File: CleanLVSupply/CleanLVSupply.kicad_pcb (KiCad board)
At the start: 4 copper layers, 40 x 40 mm, 77 parts, among them J1 12VIN, J2 5V, J3 5V, J4 5V, J5 +-15V, J6 +-15V, U1 LM25576, U2 TPS7A30, U3 LMR64010XMF, U4 TPS7A47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

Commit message: CleanLVSupply fixes, HiFiDAC skeleton
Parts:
- J5, J6: footprint BW_Connectors:Amphenol_MINITEK_0.8_3P_V -> BW_Connectors:Amphenol_MINITEK_0.8_4P_V
- R6: value 10kΩ -> 10kΩLN
- R8: value 118kΩ -> 118kΩLN
- moved C40 0.30 mm to (164.4, 116.2)
- moved C28 0.30 mm to (166.8, 105.8)
- moved C18 0.15 mm to (163.0, 91.1)
- moved C14 0.12 mm to (164.7, 83.5)
- moved J5 0.10 mm to (167.9, 98.4)
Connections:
- J5 pad 3: -15V -> GND
- J6 pad 3: -15V -> GND
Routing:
- net GND: track 138.4 -> 143.9 mm
- net +15V: track 31.2 -> 31.8 mm

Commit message: HiFiDAC schematic initially done, CleanLVSupply added shield pads
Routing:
- net GND: vias 88 -> 87

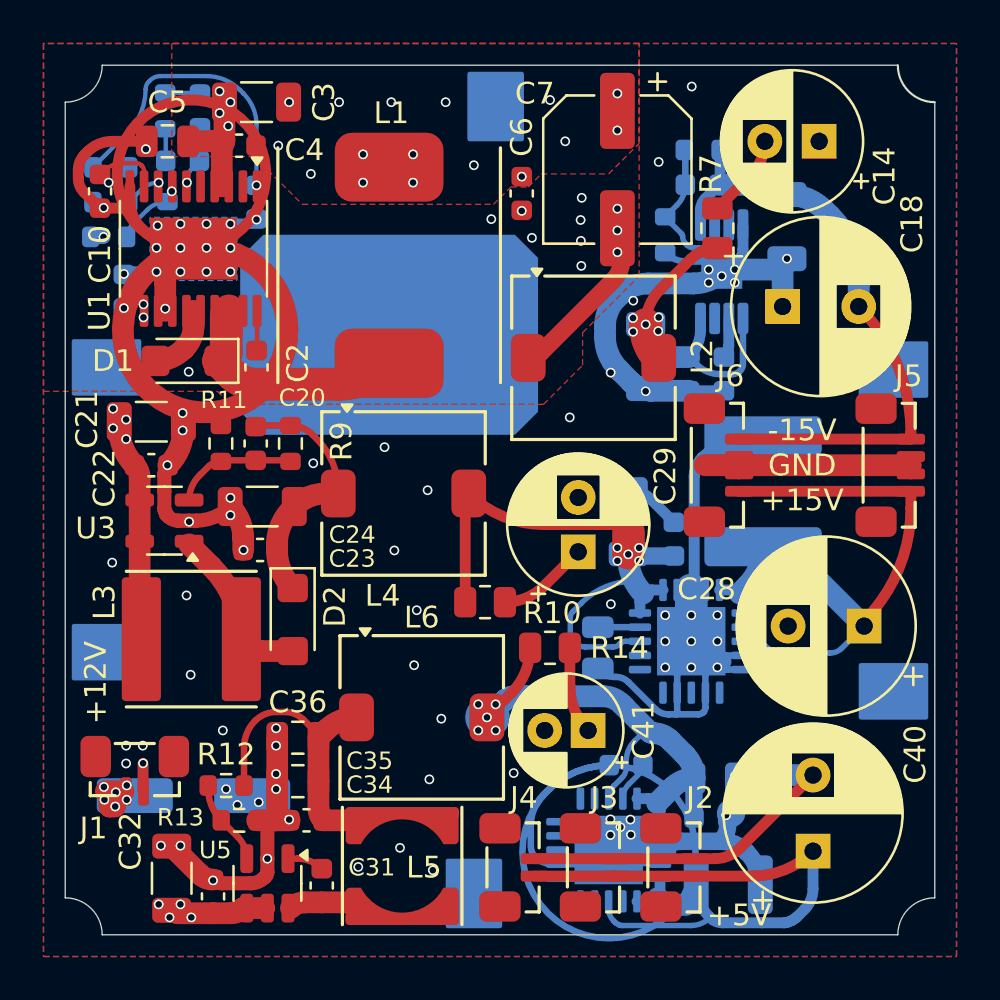
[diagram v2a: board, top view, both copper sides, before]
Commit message: HiFiDAC PCB progress, slight shape changes
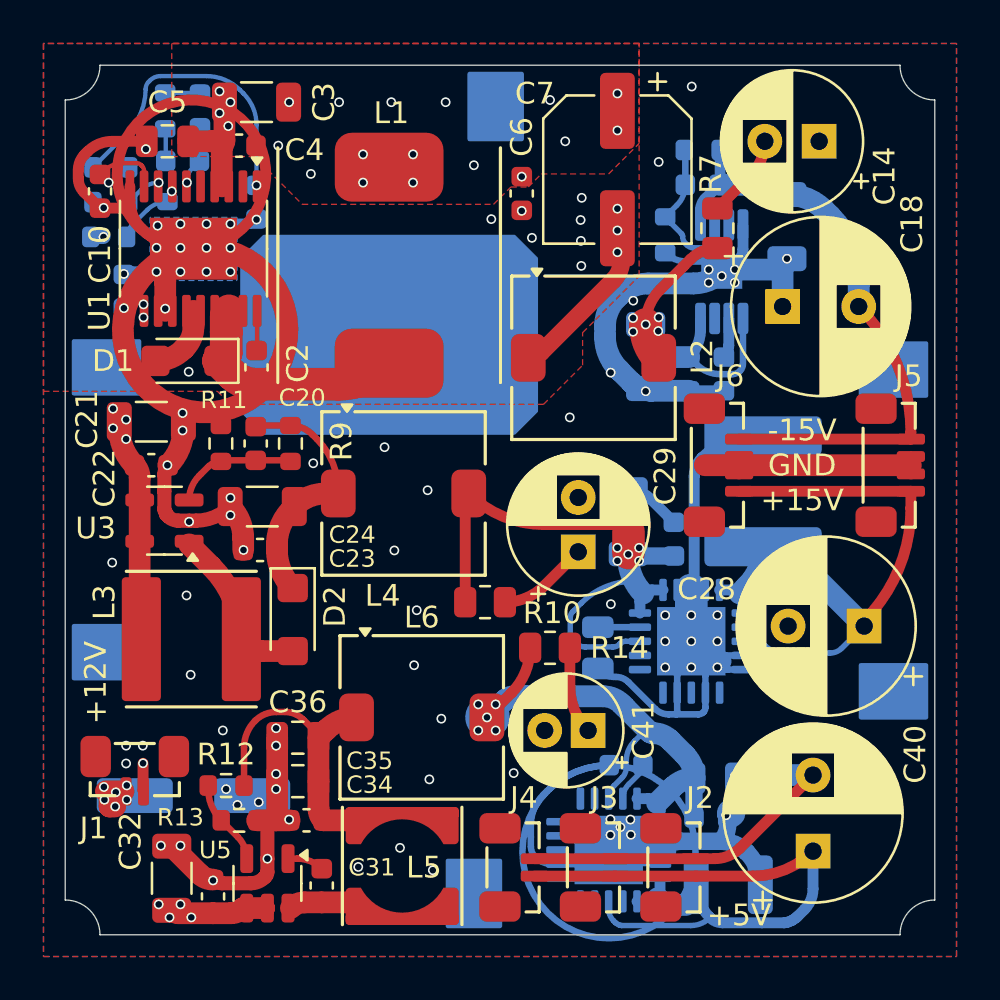
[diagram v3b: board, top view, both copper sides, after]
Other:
- outline, holes or cut-outs redrawn

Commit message: HiFiDAC routing done, CleanLVSupply fuses added
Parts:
- added F1: 375mA, Fuse:Fuse_0603_1608Metric, B.Cu at (166.2, 116.8)
- added F2: 250mA, Fuse:Fuse_0603_1608Metric, B.Cu at (168.7, 105.8)
- added F3: 250mA, Fuse:Fuse_0603_1608Metric, B.Cu at (168.7, 90.8)
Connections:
- J2 pad 1: +5V -> /5V Supply/5V_SENSE
- J3 pad 1: +5V -> /5V Supply/5V_SENSE
- J4 pad 1: +5V -> /5V Supply/5V_SENSE
- J5 pad 1: +15V -> Net-(J5-Pin_1)
- J5 pad 4: -15V -> Net-(J5-Pin_4)
- J6 pad 1: +15V -> Net-(J5-Pin_1)
- J6 pad 4: -15V -> Net-(J5-Pin_4)
- U6 pad 3: +5V -> /5V Supply/5V_SENSE
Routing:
- net /5V Supply/5V_SENSE: track 0.00 -> 28.3 mm, vias 0 -> 3
- net GND: track 143.9 -> 118.5 mm, vias 87 -> 89
- net +5V: track 32.4 -> 15.6 mm
- net Net-(J5-Pin_4): track 0.00 -> 15.5 mm, vias 0 -> 2
- net Net-(J5-Pin_1): track 0.00 -> 15.3 mm, vias 0 -> 2
- net +15V: track 31.8 -> 19.3 mm
- net -15V: track 28.4 -> 16.1 mm
